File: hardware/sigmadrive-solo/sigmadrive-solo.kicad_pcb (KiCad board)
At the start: 4 copper layers, 70.7 x 87.3 mm, 161 parts, among them J1 CONN_01X02, J10 Conn_01x03, J11 Conn_01x03, J12 Conn_01x05, J2 CONN_02X05, J4 Conn_01x05, J5 Conn_01x05, J6 629_105_150_921, J8 Conn_01x03, J9 Conn_01x03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

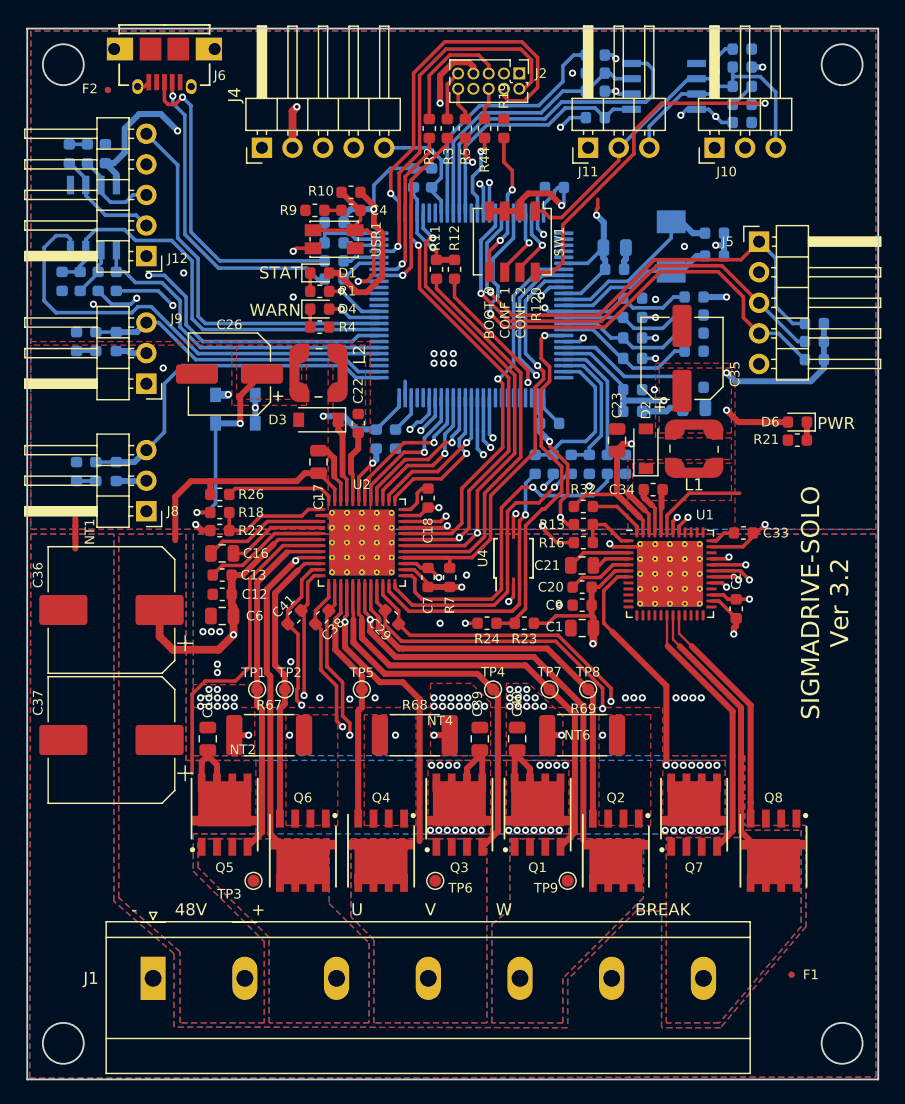
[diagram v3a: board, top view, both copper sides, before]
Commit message: Added temperature sensor.
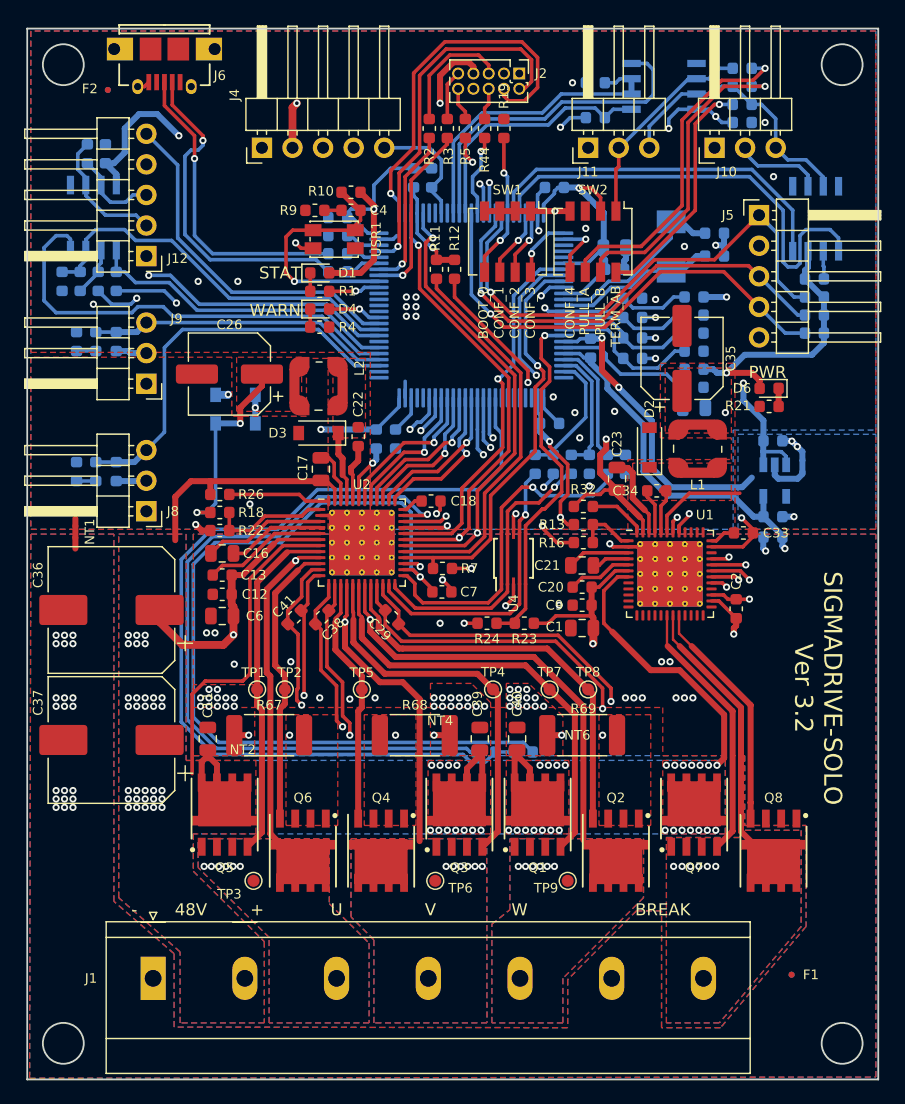
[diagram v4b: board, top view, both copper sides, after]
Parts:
- removed R36, R83: 21, Resistor_SMD:R_0603_1608Metric
- added C25: 100nF 50V, Capacitor_SMD:C_0603_1608Metric, B.Cu at (141.9, 52.7)
- added C45: 1uF 16V, Capacitor_SMD:C_0603_1608Metric, B.Cu at (138.4, 66.2)
- added C46: 2.2uF, Capacitor_SMD:C_0603_1608Metric, B.Cu at (138.4, 72.5)
- added NT3: Net-Tie_2, NetTie:NetTie-2_SMD_Pad0.5mm, B.Cu at (140.9, 68.2)
- added RV1: Varistor, Resistor_SMD:R_0603_1608Metric, B.Cu at (117.7, 92.0)
- added SW2: SW_DIP_x04, Button_Switch_SMD:SW_DIP_SPSTx04_Slide_Copal_CHS-04A_W5.08mm_P1.27mm_JPin, F.Cu at (123.5, 49.6)
- added U6: SN65HVD232DR, Package_SO:SOIC-8_3.9x4.9mm_P1.27mm, B.Cu at (142.0, 47.7)
- added U7: TPS70933, Package_TO_SOT_SMD:TSOT-23-5, B.Cu at (138.6, 69.5)
- R34: value 0 -> N/A
- R35: value 0 -> 3.3k
- R38, R40: value N/A -> 10k
- moved R35 55.6 mm to (114.6, 92.0)
- moved R34 42.7 mm to (138.4, 74.2)
- moved FB1 6.19 mm to (131.9, 60.2), turned to 0 degrees
- moved C53 4.91 mm to (123.3, 58.5), turned to 270 degrees
- moved D6 3.66 mm to (138.1, 61.8)
- moved R21 3.66 mm to (138.1, 63.3)
- moved C23 3.20 mm to (125.5, 69.3)
- moved J5 2.20 mm to (137.3, 47.4)
- moved R90 2.20 mm to (141.9, 57.2)
- moved R91 2.20 mm to (141.9, 55.7)
- moved R92 2.20 mm to (141.9, 54.2)
- moved C7 1.66 mm to (111.0, 78.7), turned to 0 degrees
- moved R38 1.60 mm to (135.9, 36.7)
- moved R40 1.60 mm to (135.9, 35.2)
- moved R88 1.50 mm to (135.9, 38.2), turned to 180 degrees
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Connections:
- net /MCU/BUSY renamed /MCU/PD2
- C51 pad 2: /MCU/PB12 -> /MCU/PB14
- C52 pad 2: /MCU/PB13 -> /MCU/PB15
- C53 pad 1: GND -> GNDA
- C53 pad 2: +3V3 -> +3.3VA
- C7 pad 1: +3V3 -> +3.3VA
- C7 pad 2: GND -> GNDA
- J8 pad 3: /MCU/PB12 -> /MCU/PB14
- J9 pad 3: /MCU/PB13 -> /MCU/PB15
- R17 pad 2: /MCU/PB12 -> /MCU/PB14
- R28 pad 2: /MCU/PB13 -> /MCU/PB15
- R34 pad 1: Net-(R34-Pad1) -> +3.3VA
- R34 pad 2: /MCU/PD3 -> +3V3
- R35 pad 1: /MCU/PD4 -> GNDA
- R35 pad 2: Net-(R34-Pad1) -> /MCU/PB0
- R38 pad 2: +3V3 -> /MCU/PULL_B
- R40 pad 1: GND -> /MCU/PULL_A
- R81 pad 2: Net-(R81-Pad2) -> Net-(J12-Pad2)
- R88 pad 2: Net-(R36-Pad1) -> /MCU/B_TERM_R120
- SW1 pad 1: /MCU/A_TERM_R120 -> +3V3
- SW1 pad 8: /MCU/B_TERM_R120 -> /MCU/GPIO_CONF_3
- U12 pad 2: Net-(R34-Pad1) -> /MCU/PD4
- U2 pad 26: +3V3 -> +3.3VA
- U2 pad 35: GND -> GNDA
- U5 pad 1: /MCU/PE2 -> /MCU/GPIO_CONF_3
- U5 pad 19: GND -> GNDA
- U5 pad 2: /MCU/PE3 -> /MCU/GPIO_CONF_4
- U5 pad 21: +3V3 -> +3.3VA
- U5 pad 62: /MCU/LED_STATUS -> /MCU/PD15
- U5 pad 66: /MCU/PC9 -> /MCU/LED_STATUS
- U5 pad 88: /MCU/PD7 -> /MCU/ENCODER_Z
- U5 pad 95: /MCU/ENCODER_Z -> /MCU/CAN_R
- U5 pad 96: /MCU/PB9 -> /MCU/CAN_D
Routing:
- net +3.3VA: track 0.00 -> 143.2 mm, vias 0 -> 2
- net GNDA: track 0.00 -> 139.1 mm, vias 0 -> 5
- net /MCU/PB0: track 0.00 -> 78.5 mm
- net /MCU/CAN_D: track 0.00 -> 38.2 mm
- net /MCU/PB14: track 0.00 -> 33.6 mm
- net /MCU/CAN_R: track 0.00 -> 30.5 mm
- net /MCU/PB12: track 29.6 -> 0.00 mm
- net /MCU/PULL_A: track 0.00 -> 27.8 mm, vias 0 -> 1
- net /MCU/PULL_B: track 0.00 -> 26.0 mm, vias 0 -> 1
- net /MCU/PB13: track 25.5 -> 0.00 mm
- net /MCU/PB15: track 0.00 -> 25.1 mm
- net /MCU/PD3: track 21.4 -> 0.00 mm
- net PGND: track 4.69 -> 25.0 mm, vias 56 -> 75
- net +5V: track 199.0 -> 211.7 mm, vias 3 -> 4
- net +3V3: track 340.5 -> 328.0 mm, vias 19 -> 18
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- added copper zone on B.Cu, net GNDA
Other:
- board text added: "CONF_3"
- board text added: "CONF_4"
- board text added: "PULL_A"
- board text added: "PULL_B"
- board text added: "TERM_AB"
- board text removed: "R120"

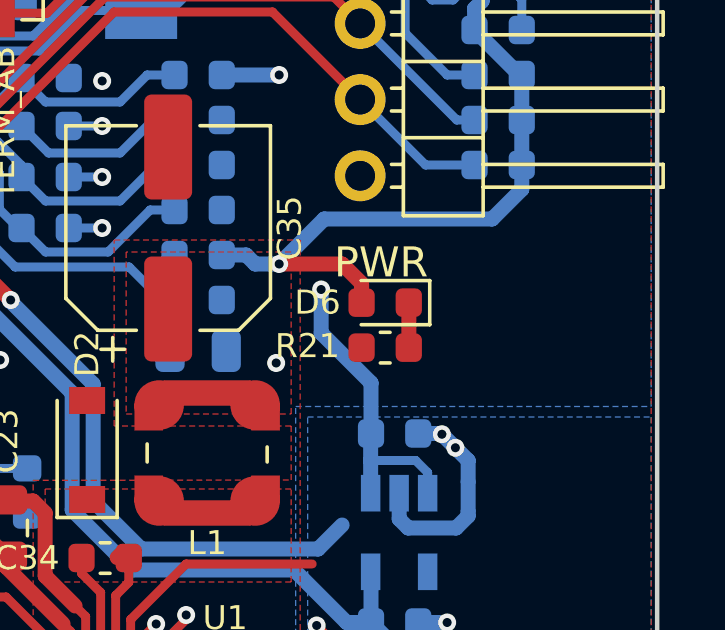
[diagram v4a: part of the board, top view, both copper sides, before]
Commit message: Updated PhoenixContact_MKDS_07x7.62mm_Vertical.kicad_mod footprint with 3D model.
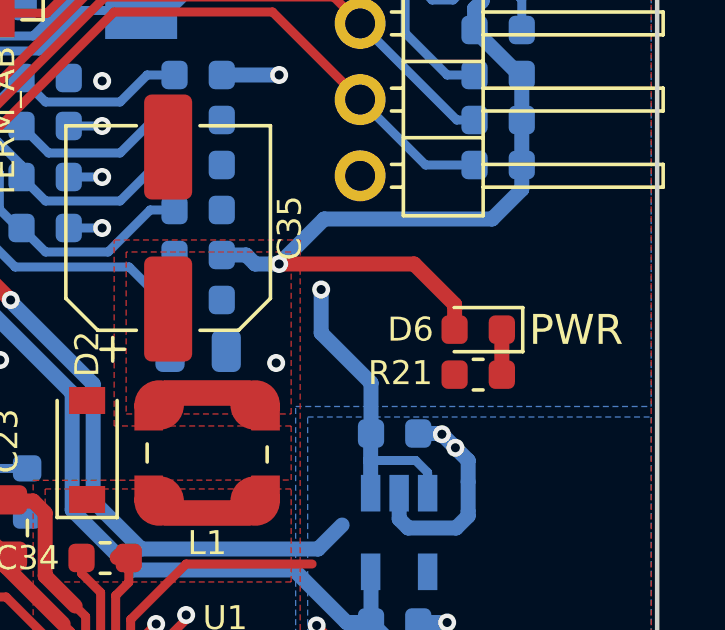
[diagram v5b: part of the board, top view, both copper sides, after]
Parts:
- moved R21 3.23 mm to (141.2, 64.2)
- moved D6 3.23 mm to (141.2, 62.7)
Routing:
- net +3V3: track 328.0 -> 331.6 mm

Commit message: Changed 18kOhm to 20kOhm part. Changed termistor value.
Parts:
- R18: value 18k -> 20k
- RV1: value Varistor -> 10K
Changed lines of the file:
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@@
   )
   (setup
-    (last_trace_width 0.3)
+    (last_trace_width 0.25)
     (user_trace_width 0.16)
     (user_trace_width 0.2)
@@
       (effects (font (size 0.8 0.8) (thickness 0.15)) (justify mirror))
     )
-    (fp_text value Varistor (at 0 -1.43 180) (layer B.Fab)
+    (fp_text value 10K (at 0 -1.43 180) (layer B.Fab)
       (effects (font (size 1 1) (thickness 0.15)) (justify mirror))
     )
@@
       (effects (font (size 0.8 0.8) (thickness 0.15)))
     )
-    (fp_text value 18k (at 0 1.43 180) (layer F.Fab)
+    (fp_text value 20k (at 0 1.43 180) (layer F.Fab)
       (effects (font (size 1 1) (thickness 0.15)))
     )

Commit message: sigmadrive-solo board 3.3
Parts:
- removed C45: 1uF 16V, Capacitor_SMD:C_0603_1608Metric
- removed C46: 2.2uF, Capacitor_SMD:C_0603_1608Metric
- removed NT3: Net-Tie_2, NetTie:NetTie-2_SMD_Pad0.5mm
- removed R34: N/A, Resistor_SMD:R_0603_1608Metric
- removed U7: TPS70933, Package_TO_SOT_SMD:TSOT-23-5
- C27, C32: value 27pF/50V/1% -> 10pF/50V/1%
- R24: value 4.7k -> 3.3k
- Y1: value ABM3-8.000MHZ-D2Y-T -> NX3225SA-12.000M-STD-CSR-1; footprint Crystal:Crystal_SMD_Abracon_ABM3-2Pin_5.0x3.2mm -> Crystal:Crystal_SMD_3225-4Pin_3.2x2.5mm
- moved F2 15.8 mm to (94.2, 48.4)
- moved F4 15.8 mm to (94.2, 48.4)
- moved C35 10.3 mm to (123.5, 66.4), turned to 180 degrees
- moved C44 7.00 mm to (119.2, 68.1)
- moved C27 6.60 mm to (127.0, 48.8), turned to 90 degrees
- moved C3 6.00 mm to (132.8, 54.5)
- moved C30 5.80 mm to (126.1, 61.9), turned to 270 degrees
- moved C34 5.49 mm to (134.2, 71.3), turned to 90 degrees
- moved D2 5.08 mm to (130.9, 71.0), turned to 180 degrees
- moved C42 5.00 mm to (125.2, 68.1)
- moved C32 4.65 mm to (129.4, 48.8), turned to 90 degrees
- moved C31 4.30 mm to (127.8, 62.1), turned to 270 degrees
- moved C2 3.96 mm to (139.1, 81.5), turned to 0 degrees
- moved C53 3.62 mm to (124.4, 61.9), turned to 90 degrees
- moved U1 3.51 mm to (133.2, 78.4)
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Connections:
- C42 pad 1: /MCU/PA2 -> /MCU/PA0
- C44 pad 1: /MCU/PA0 -> /MCU/PA2
- C53 pad 1: GNDA -> GND
- C53 pad 2: +3.3VA -> +3V3
- C7 pad 1: +3.3VA -> +3V3
- C7 pad 2: GNDA -> GND
- R24 pad 1: /MCU/VBAT_ADC -> PGND
- R24 pad 2: GND -> /MCU/VBAT_ADC
- R27 pad 2: /MOSFETs/DRV_SOA -> /MOSFETs/DRV_SOC
- R31 pad 2: /MOSFETs/DRV_SOC -> /MOSFETs/DRV_SOA
- R35 pad 1: GNDA -> GND
- RV1 pad 1: +3.3VA -> +3V3
- U2 pad 26: +3.3VA -> +3V3
- U2 pad 35: GNDA -> GND
- U5 pad 19: GNDA -> GND
- U5 pad 21: +3.3VA -> +3V3
- Y1 pad 1: Net-(C27-Pad1) -> Net-(C32-Pad1)
- Y1 pad 2: Net-(C32-Pad1) -> GND
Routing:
- net +3.3VA: track 143.2 -> 0.00 mm, vias 2 -> 0
- net GNDA: track 139.1 -> 0.00 mm, vias 5 -> 0
- net +3V3: track 331.6 -> 402.2 mm, vias 18 -> 17
- net GND: track 95.2 -> 150.2 mm, vias 37 -> 42
- net PGND: track 25.0 -> 6.11 mm, vias 75 -> 49
- net VIN: track 150.2 -> 138.5 mm, vias 69 -> 49
- net +5V: track 211.7 -> 200.7 mm, vias 4 -> 3
- net /MOSFETs/DRV_SOA: track 27.8 -> 20.7 mm
- net Net-(R12-Pad2): track 42.7 -> 47.8 mm
- net Net-(C30-Pad1): track 14.9 -> 9.89 mm
- net /MOSFETs/DRV_SOC: track 23.9 -> 28.6 mm
- net /MCU/DRV2_CS: track 42.8 -> 47.5 mm
- net /MCU/AUX_L: track 25.3 -> 29.6 mm
- net /MCU/PB14: track 33.6 -> 29.4 mm
- net /MCU/AUX_H: track 26.3 -> 30.5 mm
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- removed copper zone on B.Cu, net GNDA

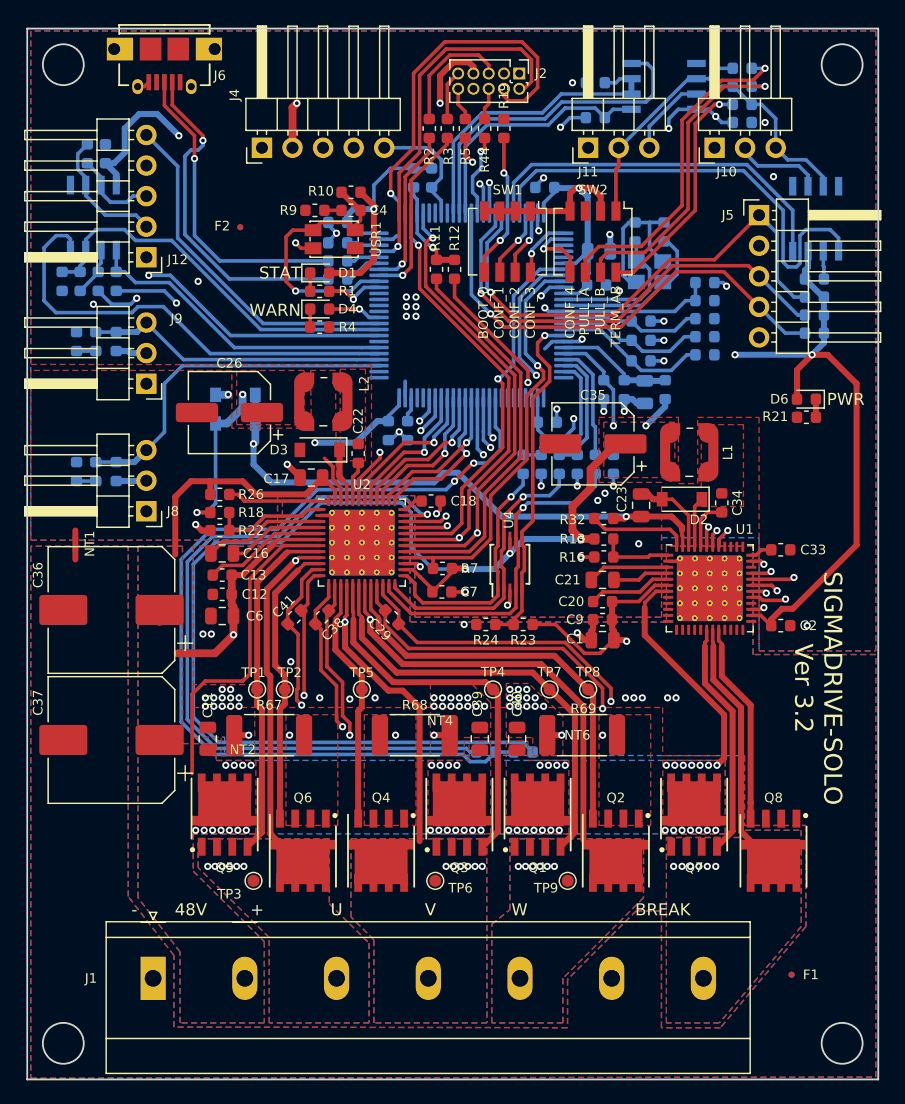
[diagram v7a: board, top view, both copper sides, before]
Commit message: added battery ADC filter.
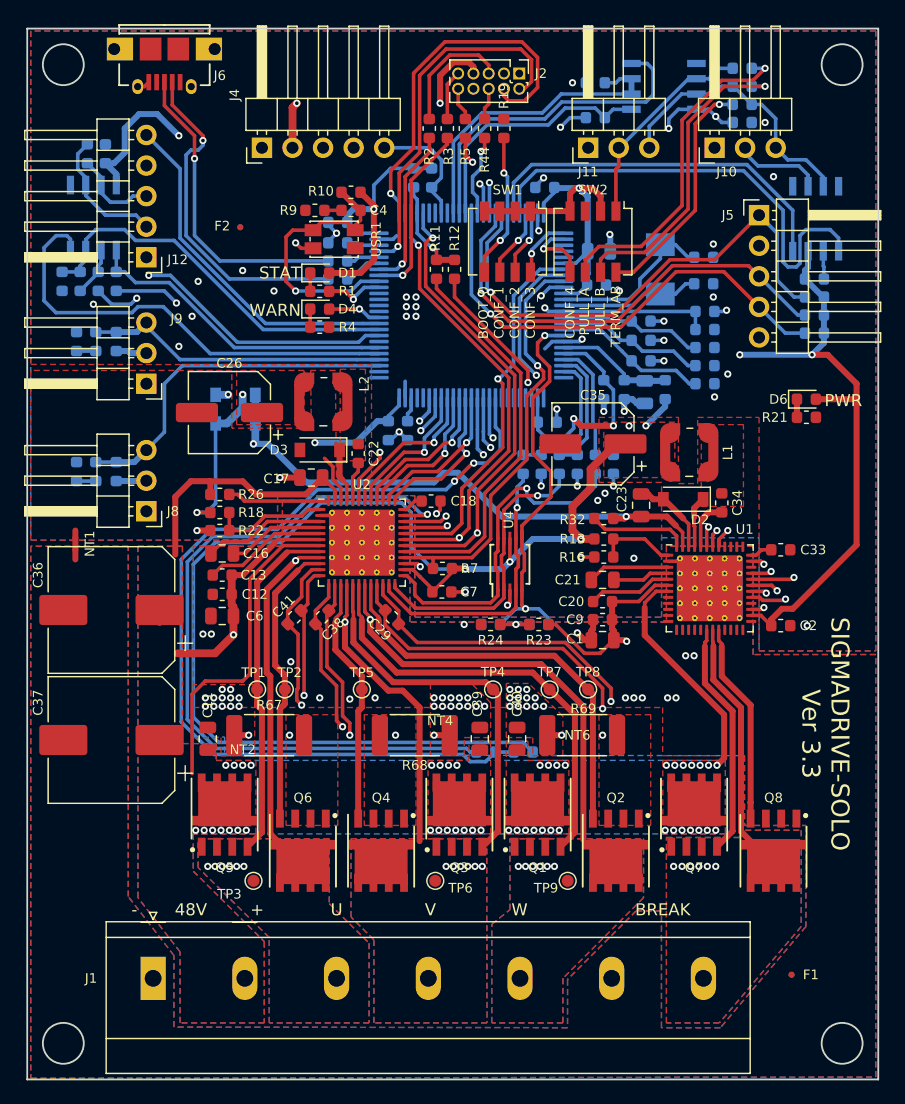
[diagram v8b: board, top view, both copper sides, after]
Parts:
- added C45: 1uF 16V, Capacitor_SMD:C_0603_1608Metric, B.Cu at (115.0, 81.4)
- added R34: 47k, Resistor_SMD:R_0603_1608Metric, B.Cu at (119.0, 81.4)
- C27, C32: value 10pF/50V/1% -> 27pF/50V/1%
- Y1: value NX3225SA-12.000M-STD-CSR-1 -> ABM3-8.000MHZ-D2Y-T; footprint Crystal:Crystal_SMD_3225-4Pin_3.2x2.5mm -> Crystal:Crystal_SMD_Abracon_ABM3-2Pin_5.0x3.2mm
- moved C27 6.07 mm to (132.7, 50.9), turned to 0 degrees
- moved C32 5.42 mm to (132.7, 53.1), turned to 0 degrees
- moved C3 2.40 mm to (132.8, 56.9)
- moved R46 2.40 mm to (132.8, 58.4)
- moved R49 2.40 mm to (132.8, 59.9)
- moved R52 2.40 mm to (132.8, 61.4)
- moved R8 2.40 mm to (132.8, 55.4)
- moved R23 1.30 mm to (119.0, 81.4)
- moved Y1 0.92 mm to (129.1, 51.9), turned to 90 degrees
- moved R24 0.40 mm to (115.0, 81.4)
- moved D2 0.10 mm to (131.0, 71.0)
- turned D6 to 0 degrees
- turned R21 to 180 degrees
- turned R68 to 180 degrees
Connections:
- R23 pad 2: /MCU/VBAT_ADC -> Net-(R23-Pad2)
- R24 pad 2: /MCU/VBAT_ADC -> Net-(R23-Pad2)
- R27 pad 2: /MOSFETs/DRV_SOC -> /MOSFETs/DRV_SOA
- R31 pad 2: /MOSFETs/DRV_SOA -> /MOSFETs/DRV_SOC
- R68 pad 1: /MOSFETs/B_ISENSE_P -> PGND
- R68 pad 2: PGND -> /MOSFETs/B_ISENSE_P
- Y1 pad 2: GND -> Net-(C27-Pad1)
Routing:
- net GND: track 150.2 -> 137.1 mm, vias 42 -> 50
- net /MOSFETs/DRV_SOA: track 20.7 -> 28.3 mm
- net /MOSFETs/DRV_SOC: track 28.6 -> 23.7 mm
- net /MCU/VBAT_ADC: track 29.2 -> 33.4 mm, vias 1 -> 2
- net Net-(R23-Pad2): track 0.00 -> 3.54 mm, vias 0 -> 1
- net Net-(C32-Pad1): track 14.0 -> 11.6 mm
- net Net-(C27-Pad1): track 12.2 -> 14.3 mm
- net VIN: track 138.5 -> 137.2 mm
- net +5V: track 200.7 -> 199.4 mm
- net +3V3: track 402.2 -> 401.2 mm, vias 17 -> 18
- net PGND: vias 49 -> 51
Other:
- board text added: "SIGMADRIVE-SOLO Ver 3.3"
- board text removed: "SIGMADRIVE-SOLO Ver 3.2"
